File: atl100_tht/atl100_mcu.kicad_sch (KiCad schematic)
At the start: 9 parts

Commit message: feat: Version 1.0.0
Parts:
- removed R10, R4, R8: 10k, symbol Device:R
- removed R3, R5: 4.7k, symbol Device:R
- R6: value 10k -> 4.7k; footprint (none) -> Resistor_THT:R_Axial_DIN0207_L6.3mm_D2.5mm_P10.16mm_Horizontal; Manufacturer (none) -> Std; Part Number (none) -> Std
- R7, R9: footprint (none) -> Resistor_THT:R_Axial_DIN0207_L6.3mm_D2.5mm_P10.16mm_Horizontal; Manufacturer (none) -> Std; Part Number (none) -> Std
- U2: value ~ -> ESP32-S3 DevKit; Manufacturer (none) -> OEM; Part Number (none) -> AI-S3
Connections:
- net +3V3: no longer R7.1, R9.1
- net ADC_ALERT: now also U2.28 (MTMS/GPIO42); no longer U2.5 (GPIO5/RTC_GPIO5/ADC1_CH4)
- net AN-: now also R7.2, U2.35 (SUBSPID/FSPID/SPIIO6/GPIO35); no longer U2.14 (GPIO46)
- net GND: now also R7.1, R9.2
- net I2C_SDA: no longer R9.2
- net LED_BLUE: now also U2.6 (GPIO6/RTC_GPIO6/ADC1_CH5); no longer U2.13 (GPIO3/RTC_GPIO3/ADC1_CH2)
- net LED_GREEN: now also U2.8 (GPIO15/RTC_GPIO15/ADC2_CH4/U0RTS); no longer U2.40 (RTC_GPIO21/GPIO21)
- net LED_RED: now also U2.7 (GPIO7/RTC_GPIO7/ADC1_CH6); no longer U2.36 (RTC_GPIO0/GPIO0)
- net MCU_TXD - RS485_RXD: no longer R7.2
- net PL-: now also R9.1, U2.30 (MTDO/GPIO40); no longer R6.2, U2.37 (GPIO45)
- net PWR_SENSOR: now also U2.20 (GPIO14/RTC_GPIO14/ADC2_CH3/FSPIWP/FSPIDQS/SUBSPIWP); no longer U2.42 (USB_D-/U1RTS/ADC2_CH8/RTC_GPIO19/GPIO19)
- net WS-: now also R6.2, U2.40 (RTC_GPIO21/GPIO21); no longer U2.6 (GPIO6/RTC_GPIO6/ADC1_CH5)
- net MCU_TXD - LTE_RXD: now reaches U2.10 (GPIO17/RTC_GPIO17/ADC2_CH6/U1TXD)
- net MCU_RXD - LTE_TXD: now reaches U2.11 (GPIO18/RTC_GPIO18/ADC2_CH7/U1RXD)
- net DS18B20_DATA: no longer names the net of U2.4 (GPIO4/RTC_GPIO4/ADC1_CH3)
- net HD38_A0: no longer names the net of U2.41 (USB_D+/U1CTS/ADC2_CH9/RTC_GPIO20/GPIO20)

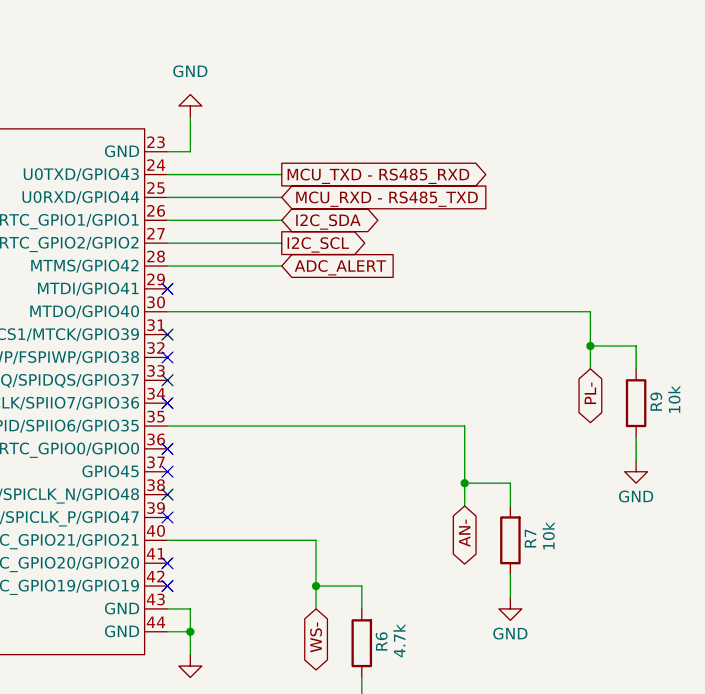
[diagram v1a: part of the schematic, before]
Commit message: feat: Updated pins to RS-485 UART
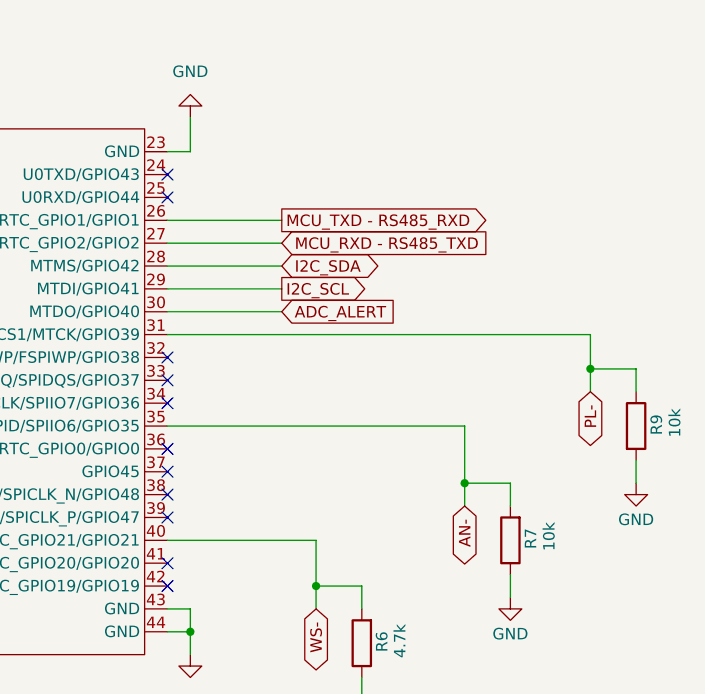
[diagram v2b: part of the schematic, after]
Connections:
- net ADC_ALERT: now also U2.30 (MTDO/GPIO40); no longer U2.28 (MTMS/GPIO42)
- net I2C_SCL: now also U2.29 (MTDI/GPIO41); no longer U2.27 (ADC1_CH1/RTC_GPIO2/GPIO2)
- net I2C_SDA: now also U2.28 (MTMS/GPIO42); no longer U2.26 (ADC1_CH0/RTC_GPIO1/GPIO1)
- net MCU_RXD - RS485_TXD: now also U2.27 (ADC1_CH1/RTC_GPIO2/GPIO2); no longer U2.25 (U0RXD/GPIO44)
- net MCU_TXD - RS485_RXD: now also U2.26 (ADC1_CH0/RTC_GPIO1/GPIO1); no longer U2.24 (U0TXD/GPIO43)
- net PL-: now also U2.31 (SUBSPICS1/MTCK/GPIO39); no longer U2.30 (MTDO/GPIO40)
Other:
- moved on the sheet: R9
